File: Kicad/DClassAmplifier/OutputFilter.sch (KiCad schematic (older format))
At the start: 5 parts

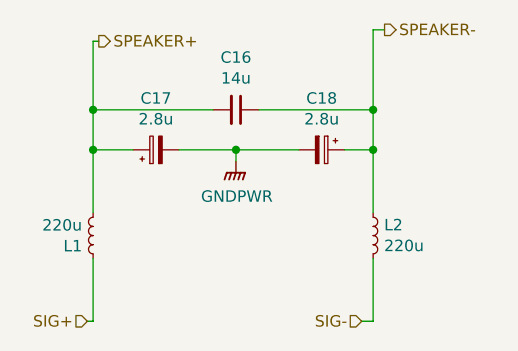
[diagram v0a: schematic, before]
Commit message: Add 10V Reg and Reroute
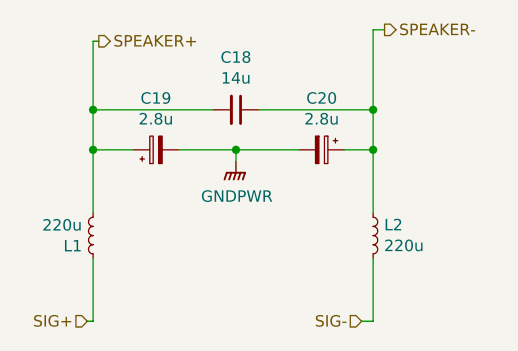
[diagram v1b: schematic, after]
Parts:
- renumbered C16 to C18, C17 to C19, C18 to C20
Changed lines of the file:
@@
 $EndComp
 $Comp
-L Device:C_Small C16
+L Device:C_Small C18
 U 1 1 61156022
 P 5375 2675
-F 0 "C16" V 5146 2675 50  0000 C CNN
+F 0 "C18" V 5146 2675 50  0000 C CNN
 F 1 "14u" V 5237 2675 50  0000 C CNN
 F 2 "OutputFilmCapacitor:C4AQLBU5140M18K" H 5375 2675 50  0001 C CNN
@@
 $EndComp
 $Comp
-L Device:CP_Small C18
+L Device:CP_Small C20
 U 1 1 61156A03
 P 5750 2850
-F 0 "C18" V 5525 2850 50  0000 C CNN
+F 0 "C20" V 5525 2850 50  0000 C CNN
 F 1 "2.8u" V 5616 2850 50  0000 C CNN
 F 2 "Capacitor_THT:CP_Radial_D8.0mm_P3.50mm" H 5750 2850 50  0001 C CNN
@@
 	5975 3600 5925 3600
 $Comp
-L power:GNDPWR #PWR049
+L power:GNDPWR #PWR052
 U 1 1 6115D61E
 P 5375 2900
-F 0 "#PWR049" H 5375 2700 50  0001 C CNN
+F 0 "#PWR052" H 5375 2700 50  0001 C CNN
 F 1 "GNDPWR" H 5379 2746 50  0000 C CNN
 F 2 "" H 5375 2850 50  0001 C CNN
@@
 	5375 2850 5650 2850
 $Comp
-L Device:CP_Small C17
+L Device:CP_Small C19
 U 1 1 61203FC8
 P 5025 2850
-F 0 "C17" V 5250 2850 50  0000 C CNN
+F 0 "C19" V 5250 2850 50  0000 C CNN
 F 1 "2.8u" V 5159 2850 50  0000 C CNN
 F 2 "Capacitor_THT:CP_Radial_D8.0mm_P3.50mm" H 5025 2850 50  0001 C CNN
